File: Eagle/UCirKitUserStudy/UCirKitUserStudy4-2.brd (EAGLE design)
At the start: 83.8 x 94.3 mm, 30 parts, among them IC1 74595DIL16-OVAL-PIN, IC2 LM35TO92-EXPANDED-OVAL-PIN

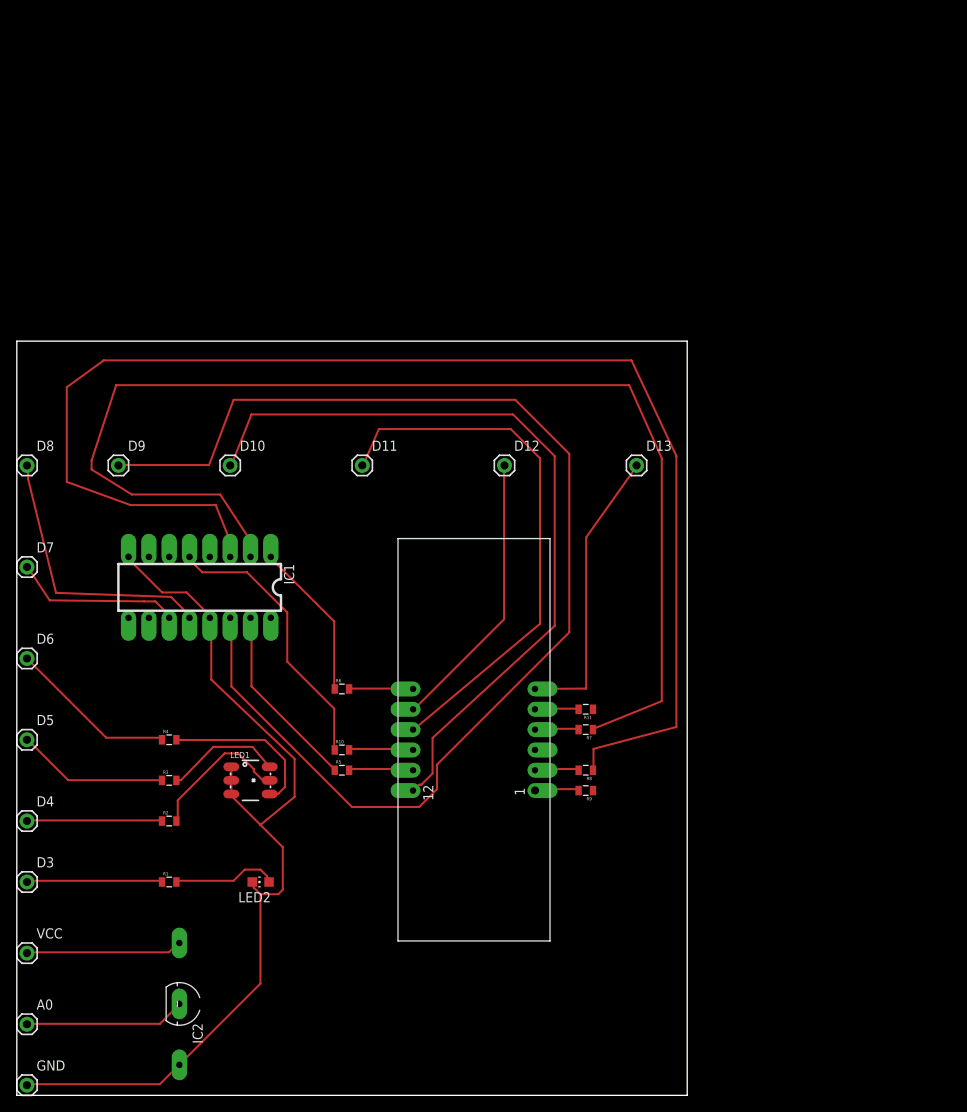
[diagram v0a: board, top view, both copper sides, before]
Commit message: UCirKitUserStudy4-2 and UCirKitUserStudy5-2 introduces 90 degree male headers for jumper wires
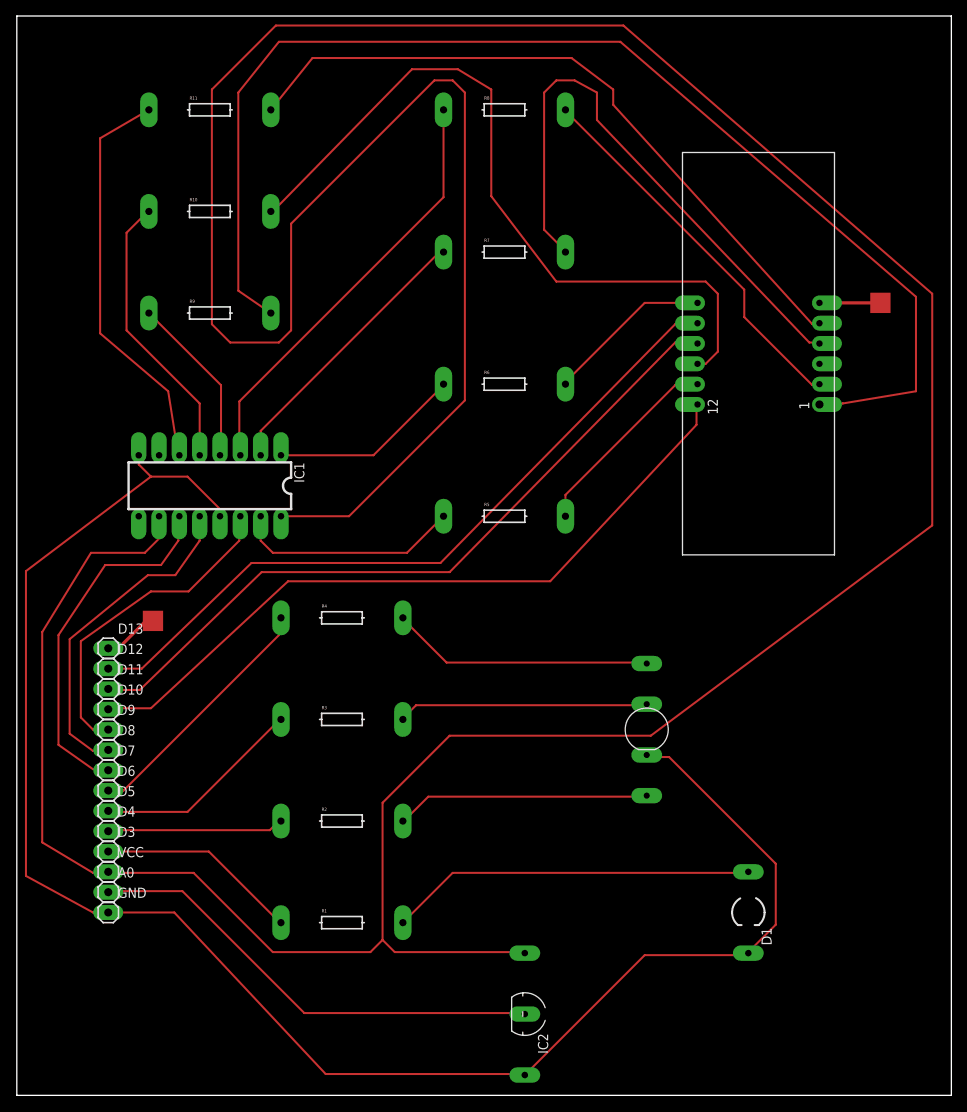
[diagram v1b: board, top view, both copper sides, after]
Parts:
- removed LED1: LED-TRICOLOR-5050NO_IC, SparkFun-LED:LED-TRICOLOR-5050
- removed LED2: (no value), led:CHIP-LED0805
- added D1: (no value), SparkFun-LED:LED3MM-EXPANDED-OVAL-PIN
- added D2: LED-RGB-CC-THRULED-RGB-THRU-EXPANDED-OVAL-PIN, SparkFun-LED:LED-RGB-THRU-EXPANDED-OVAL-PIN
- A0, D10, D11, D12, D13, D3, D4, D5, D6, D7, D8, D9, GND, VCC: device SparkFun-Connectors:1X01 -> SparkFun-Connectors:1X01_OVAL_PIN
- R1, R10, R11, R2, R3, R4, R5, R6, R7, R8, R9: value 0.3 -> (none); device SparkFun-Resistors:0805 -> SparkFun-Resistors:PTH-EXPANDED-OVAL-PIN
- moved R11 88.4 mm to (24.1, 123.2), turned to 0 degrees
- moved R8 83.2 mm to (61.0, 123.2), turned to 0 degrees
- moved R9 76.0 mm to (24.1, 97.8), turned to 0 degrees
- moved D13 69.9 mm to (11.4, 55.9)
- moved R10 69.3 mm to (24.1, 110.5)
- moved R7 60.5 mm to (61.0, 105.4), turned to 0 degrees
- moved U$1 59.9 mm to (92.7, 92.7)
- moved D12 55.7 mm to (11.4, 53.3)
- moved IC2 43.2 mm to (63.5, 10.2)
- moved R6 43.2 mm to (61.0, 88.9)
- moved D11 42.3 mm to (11.4, 50.8)
- moved R5 37.7 mm to (61.0, 72.4)
- moved D8 37.0 mm to (11.4, 43.2)
- moved D10 34.1 mm to (11.4, 48.3)
- moved D9 33.0 mm to (11.4, 45.7)
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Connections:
- net A: now also R5.P$1; no longer R5.1
- net B: now also R6.P$1; no longer R6.1
- net C: now also R7.P$1; no longer R7.1
- net D: now also R8.P$1; no longer R8.1
- net D3: now also R1.P$1; no longer R1.1
- net D4: now also R2.P$1; no longer R2.1
- net D5: now also R3.P$1; no longer R3.1
- net D6: now also R4.P$1; no longer R4.1
- net E: now also R9.P$1; no longer R9.1
- net F: now also R10.P$1; no longer R10.1
- net G: now also R11.P$1; no longer R11.1
- net GND: now also D1.K, D2.2; no longer LED1.1, LED1.2, LED1.3, LED2.C
- net N$1: now also D1.A, R1.P$2; no longer R5.2, U$1.11
- net N$10: now also R10.P$2, U$1.10; no longer LED1.4, R4.2
- net N$11: now also R11.P$2, U$1.5; no longer LED2.A, R1.2
- net N$2: now also D2.1, R2.P$2; no longer R6.2, U$1.7
- net N$3: now also D2.3, R3.P$2; no longer R7.2, U$1.4
- net N$4: now also D2.4, R4.P$2; no longer R8.2, U$1.2
- net N$5: now also R5.P$2, U$1.11; no longer R9.2, U$1.1
- net N$6: now also R6.P$2, U$1.7; no longer R10.2, U$1.10
- net N$7: now also R7.P$2, U$1.4; no longer R11.2, U$1.5
- net N$8: now also R8.P$2, U$1.2; no longer LED1.5, R2.2
- net N$9: now also R9.P$2, U$1.1; no longer LED1.6, R3.2
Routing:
- net VCC: track 19.6 -> 501.3 mm
- net N$9: track 14.6 -> 153.3 mm
- net D: track 170.0 -> 53.9 mm
- net C: track 150.8 -> 35.3 mm
- net D9: track 155.1 -> 41.2 mm
- net GND: track 114.9 -> 213.5 mm
- net N$11: track 13.2 -> 87.1 mm
- net N$10: track 20.2 -> 93.7 mm
- net N$7: track 5.52 -> 71.9 mm
- net D12: track 35.3 -> 91.6 mm
- net G: track 0.00 -> 50.8 mm
- net A0: track 20.1 -> 58.5 mm
- net N$1: track 8.17 -> 45.9 mm
- net N$8: track 18.2 -> 48.1 mm
- net N$4: track 5.65 -> 32.9 mm
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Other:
- board size 83.8 x 94.3 mm -> 116.8 x 134.9 mm
